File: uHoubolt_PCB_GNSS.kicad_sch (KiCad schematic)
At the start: 88 parts, among them J1 Power In, J12 MMCX-J-P-H-RA-SM1, J2 Debug, J3 Debug, J4 CAN1, J5 CAN2, J6 CAN1, J7 CAN2, Q1 SISA88DN or similar, U1 SAM-M8Q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

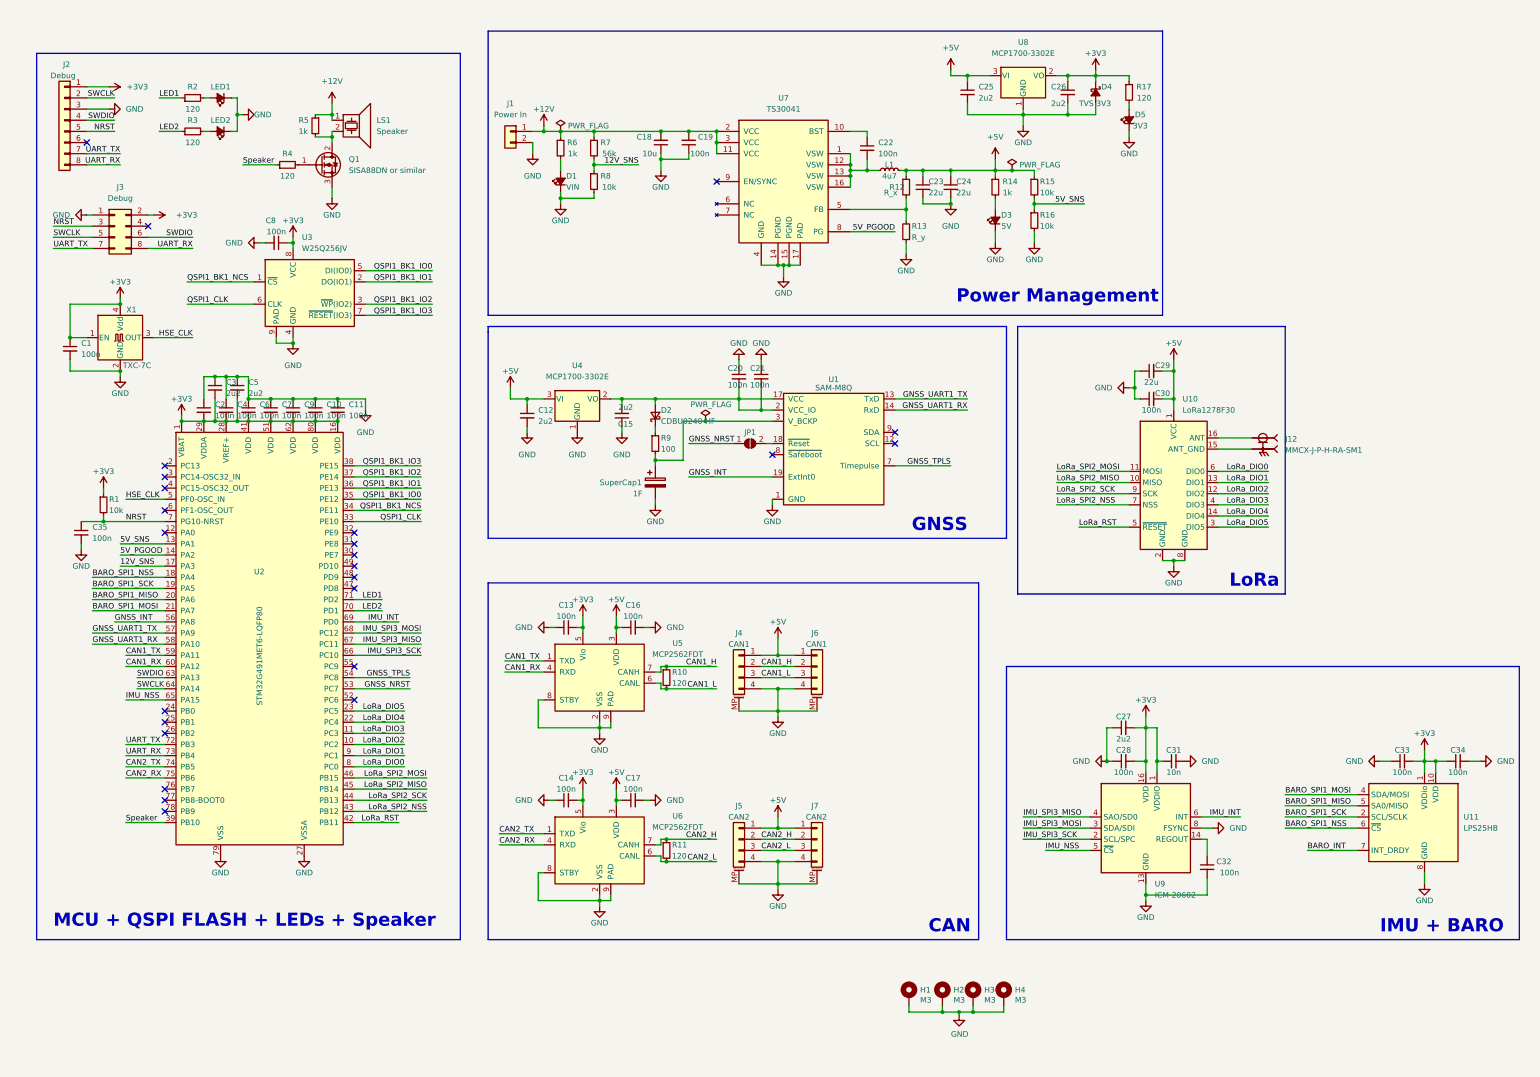
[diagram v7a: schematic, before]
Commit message: Fixed BARO INT and updated footprints for big caps
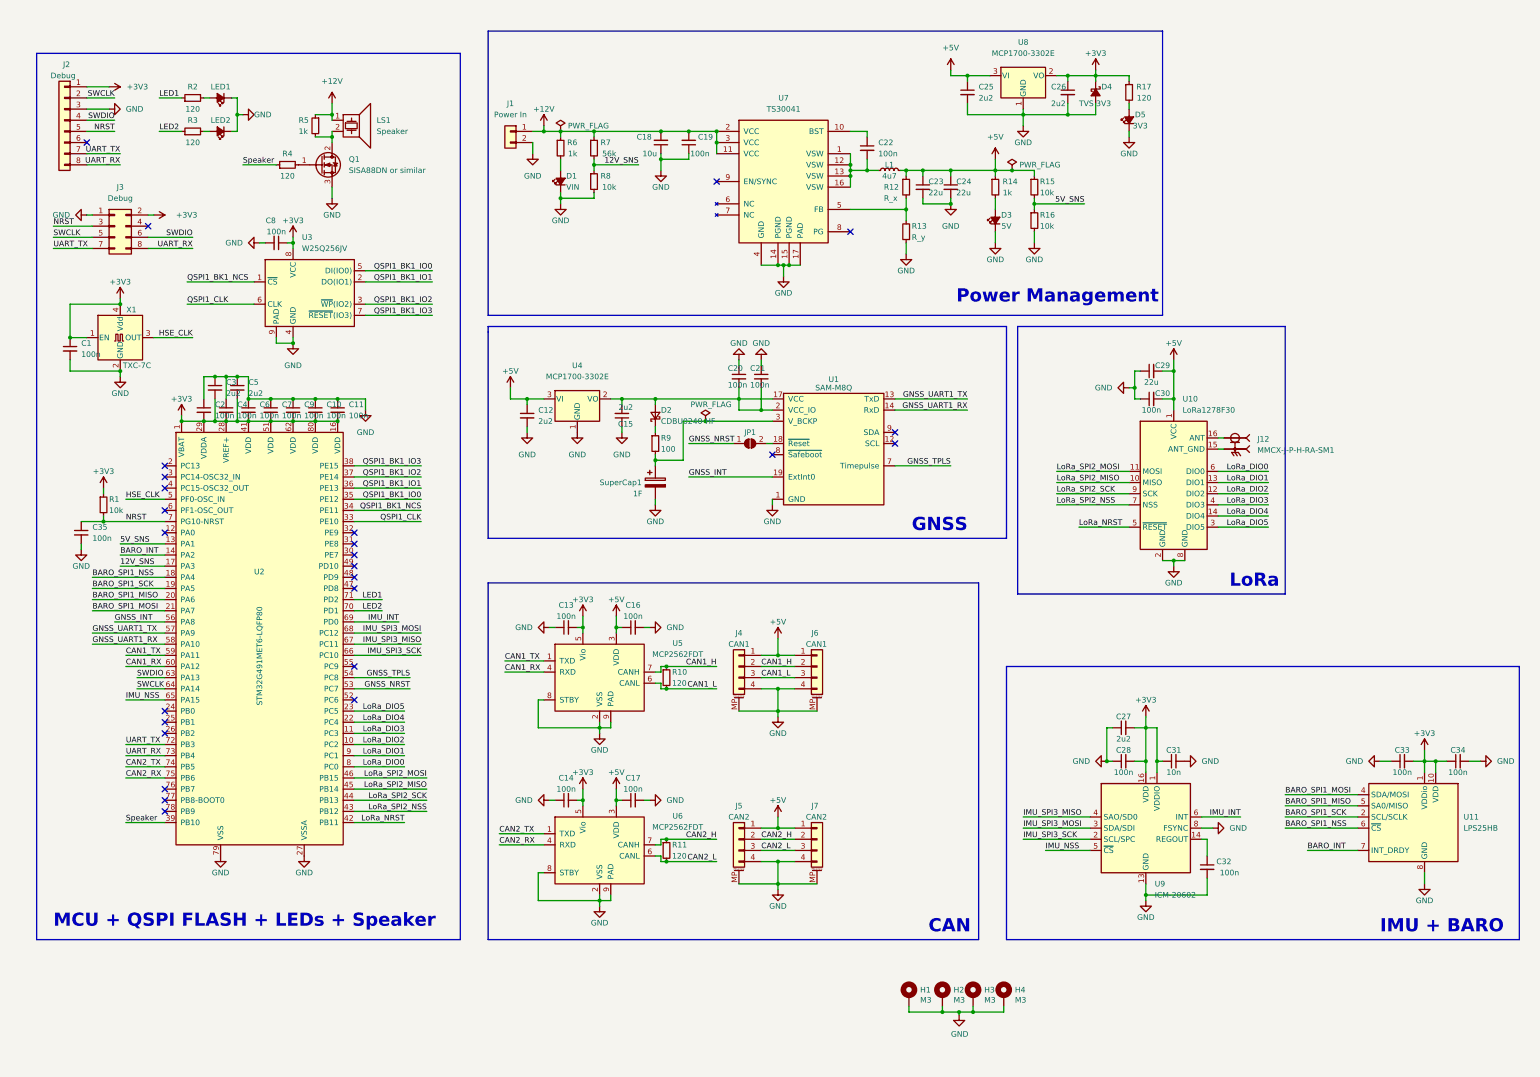
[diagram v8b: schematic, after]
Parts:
- C23, C24: footprint Capacitor_SMD:C_0603_1608Metric -> Capacitor_SMD:C_0805_2012Metric
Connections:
- net BARO_INT: now also U2.14 (PA2)
- net 5V_PGOOD: no longer names the net of U7.8 (PG)
- net 5V_PGOOD: no longer U2.14 (PA2)
- net LoRa_RST renamed LoRa_NRST
- no-connect marks 25 -> 26
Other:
- moved on the sheet: J12
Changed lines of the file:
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@@
   )
   (no_connect (at 234.95 139.7))
+  (no_connect (at 252.73 88.9))
   (no_connect (at 96.52 152.4))
   (no_connect (at 78.74 68.58))
@@
     (stroke (width 0) (type default) (color 0 0 0 0))
   )
+  (wire (pts (xy 86.36 162.56) (xy 96.52 162.56))
+    (stroke (width 0) (type default) (color 0 0 0 0))
+  )
   (wire (pts (xy 139.7 193.04) (xy 152.4 193.04))
     (stroke (width 0) (type default) (color 0 0 0 0))
@@
     (stroke (width 0) (type default) (color 0 0 0 0))
   )
-  (wire (pts (xy 139.7 223.52) (xy 149.86 223.52))
+  (wire (pts (xy 139.7 223.52) (xy 151.13 223.52))
     (stroke (width 0) (type default) (color 0 0 0 0))
   )
@@
     (stroke (width 0) (type default) (color 0 0 0 0))
   )
-  (wire (pts (xy 262.89 88.9) (xy 252.73 88.9))
-    (stroke (width 0) (type default) (color 0 0 0 0))
-  )
   (wire (pts (xy 182.88 195.58) (xy 181.61 195.58))
     (stroke (width 0) (type default) (color 0 0 0 0))
@@
     (stroke (width 0) (type default) (color 0 0 0 0))
   )
-  (wire (pts (xy 86.36 162.56) (xy 96.52 162.56))
-    (stroke (width 0) (type default) (color 0 0 0 0))
-  )
   (wire (pts (xy 252.73 71.12) (xy 252.73 73.66))
     (stroke (width 0) (type default) (color 0 0 0 0))
@@
     (stroke (width 0) (type default) (color 0 0 0 0))
   )
-  (wire (pts (xy 336.55 135.89) (xy 344.17 135.89))
+  (wire (pts (xy 336.55 135.89) (xy 337.82 135.89))
     (stroke (width 0) (type default) (color 0 0 0 0))
   )
@@
     (stroke (width 0) (type default) (color 0 0 0 0))
   )
-  (wire (pts (xy 336.55 138.43) (xy 344.17 138.43))
+  (wire (pts (xy 336.55 138.43) (xy 337.82 138.43))
     (stroke (width 0) (type default) (color 0 0 0 0))
   )
@@
     (effects (font (size 1.27 1.27)) (justify right bottom))
   )
-  (label "LoRa_RST" (at 149.86 223.52 180)
+  (label "LoRa_NRST" (at 151.13 223.52 180)
     (effects (font (size 1.27 1.27)) (justify right bottom))
   )
@@
     (effects (font (size 1.27 1.27)) (justify right bottom))
   )
-  (label "5V_PGOOD" (at 86.36 162.56 0)
-    (effects (font (size 1.27 1.27)) (justify left bottom))
-  )
   (label "CAN1_H" (at 222.25 187.96 180)
     (effects (font (size 1.27 1.27)) (justify right bottom))
@@
     (effects (font (size 1.27 1.27)) (justify right bottom))
   )
-  (label "5V_PGOOD" (at 262.89 88.9 180)
-    (effects (font (size 1.27 1.27)) (justify right bottom))
-  )
   (label "SWCLK" (at 71.12 90.17 0)
     (effects (font (size 1.27 1.27)) (justify left bottom))
@@
     (effects (font (size 1.27 1.27)) (justify right bottom))
   )
+  (label "BARO_INT" (at 86.36 162.56 0)
+    (effects (font (size 1.27 1.27)) (justify left bottom))
+  )
   (label "CAN2_RX" (at 87.63 213.36 0)
     (effects (font (size 1.27 1.27)) (justify left bottom))
@@
     (effects (font (size 1.27 1.27)) (justify right bottom))
   )
-  (label "LoRa_RST" (at 304.8 156.21 0)
+  (label "LoRa_NRST" (at 304.8 156.21 0)
     (effects (font (size 1.27 1.27)) (justify left bottom))
   )
@@
     (pin "2")
   )
-  (symbol (lib_id "TXV_Library_Symbols:MMCX-J-P-H-RA-SM1") (at 346.71 138.43 0) (mirror y) (unit 1)
+  (symbol (lib_id "TXV_Library_Symbols:MMCX-J-P-H-RA-SM1") (at 340.36 138.43 0) (mirror y) (unit 1)
     (in_bom yes) (on_board yes) (fields_autoplaced)
-    (property "Reference" "J12" (id 0) (at 351.79 136.1439 0)
+    (property "Reference" "J12" (id 0) (at 345.44 136.1439 0)
       (effects (font (size 1.27 1.27)) (justify right))
     )
-    (property "Value" "MMCX-J-P-H-RA-SM1" (id 1) (at 351.79 138.6839 0)
+    (property "Value" "MMCX-J-P-H-RA-SM1" (id 1) (at 345.44 138.6839 0)
       (effects (font (size 1.27 1.27)) (justify right))
     )
-    (property "Footprint" "SAMTEC_MMCX-J-P-H-RA-SM1" (id 2) (at 346.71 138.43 0)
+    (property "Footprint" "SAMTEC_MMCX-J-P-H-RA-SM1" (id 2) (at 340.36 138.43 0)
       (effects (font (size 1.27 1.27)) (justify left bottom) hide)
     )
-    (property "Datasheet" "" (id 3) (at 346.71 138.43 0)
+    (property "Datasheet" "" (id 3) (at 340.36 138.43 0)
       (effects (font (size 1.27 1.27)) (justify left bottom) hide)
     )
-    (property "STANDARD" "Manufacturer Recommendations" (id 4) (at 346.71 138.43 0)
+    (property "STANDARD" "Manufacturer Recommendations" (id 4) (at 340.36 138.43 0)
       (effects (font (size 1.27 1.27)) (justify left bottom) hide)
     )
-    (property "MANUFACTURER" "Samtec" (id 5) (at 346.71 138.43 0)
+    (property "MANUFACTURER" "Samtec" (id 5) (at 340.36 138.43 0)
       (effects (font (size 1.27 1.27)) (justify left bottom) hide)
     )
-    (property "MAXIMUM_PACKAGE_HEIGHT" "4.6mm" (id 6) (at 346.71 138.43 0)
+    (property "MAXIMUM_PACKAGE_HEIGHT" "4.6mm" (id 6) (at 340.36 138.43 0)
       (effects (font (size 1.27 1.27)) (justify left bottom) hide)
     )
-    (property "PARTREV" "F" (id 7) (at 346.71 138.43 0)
+    (property "PARTREV" "F" (id 7) (at 340.36 138.43 0)
       (effects (font (size 1.27 1.27)) (justify left bottom) hide)
     )
@@
       (effects (font (size 1.27 1.27)) (justify left))
     )
-    (property "Footprint" "Capacitor_SMD:C_0603_1608Metric" (id 2) (at 275.59 78.74 0)
+    (property "Footprint" "Capacitor_SMD:C_0805_2012Metric" (id 2) (at 275.59 78.74 0)
       (effects (font (size 1.27 1.27)) hide)
     )
@@
       (effects (font (size 1.27 1.27)) (justify left))
     )
-    (property "Footprint" "Capacitor_SMD:C_0603_1608Metric" (id 2) (at 269.24 78.74 0)
+    (property "Footprint" "Capacitor_SMD:C_0805_2012Metric" (id 2) (at 269.24 78.74 0)
       (effects (font (size 1.27 1.27)) hide)
     )
@@
   (symbol (lib_id "Device:R_Small") (at 265.43 78.74 0) (unit 1)
     (in_bom yes) (on_board yes)
-    (property "Reference" "R12" (id 0) (at 261.62 78.74 0)
+    (property "Reference" "R12" (id 0) (at 260.35 78.74 0)
       (effects (font (size 1.27 1.27)) (justify left))
     )
-    (property "Value" "R_x" (id 1) (at 260.35 80.01 0)
+    (property "Value" "R_x" (id 1) (at 260.35 81.28 0)
       (effects (font (size 1.27 1.27)) (justify left))
     )
@@
     )
     (path "/59e81957-7697-4a00-b577-11c972f2a000"
-      (reference "C23") (unit 1) (value "22u") (footprint "Capacitor_SMD:C_0603_1608Metric")
+      (reference "C23") (unit 1) (value "22u") (footprint "Capacitor_SMD:C_0805_2012Metric")
     )
     (path "/4fa95f34-06aa-4263-ab8d-4f021381e32d"
-      (reference "C24") (unit 1) (value "22u") (footprint "Capacitor_SMD:C_0603_1608Metric")
+      (reference "C24") (unit 1) (value "22u") (footprint "Capacitor_SMD:C_0805_2012Metric")
     )
     (path "/c8bb61dc-798c-4bb7-a45f-653284ed0726"
